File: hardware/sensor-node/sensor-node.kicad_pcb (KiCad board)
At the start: 2 copper layers, 57 x 57 mm, 52 parts, among them J1 CONUFL001-SMD-T, J2 Conn_ARM_JTAG_SWD_10, Q1 PMV250EPEA, U1 TLV61225, U2 TPS27081A, U3 SHT31-DIS, U4 24LC32, U5 MLX90614, U6 ADG633YRU, U7 TSV911RILT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

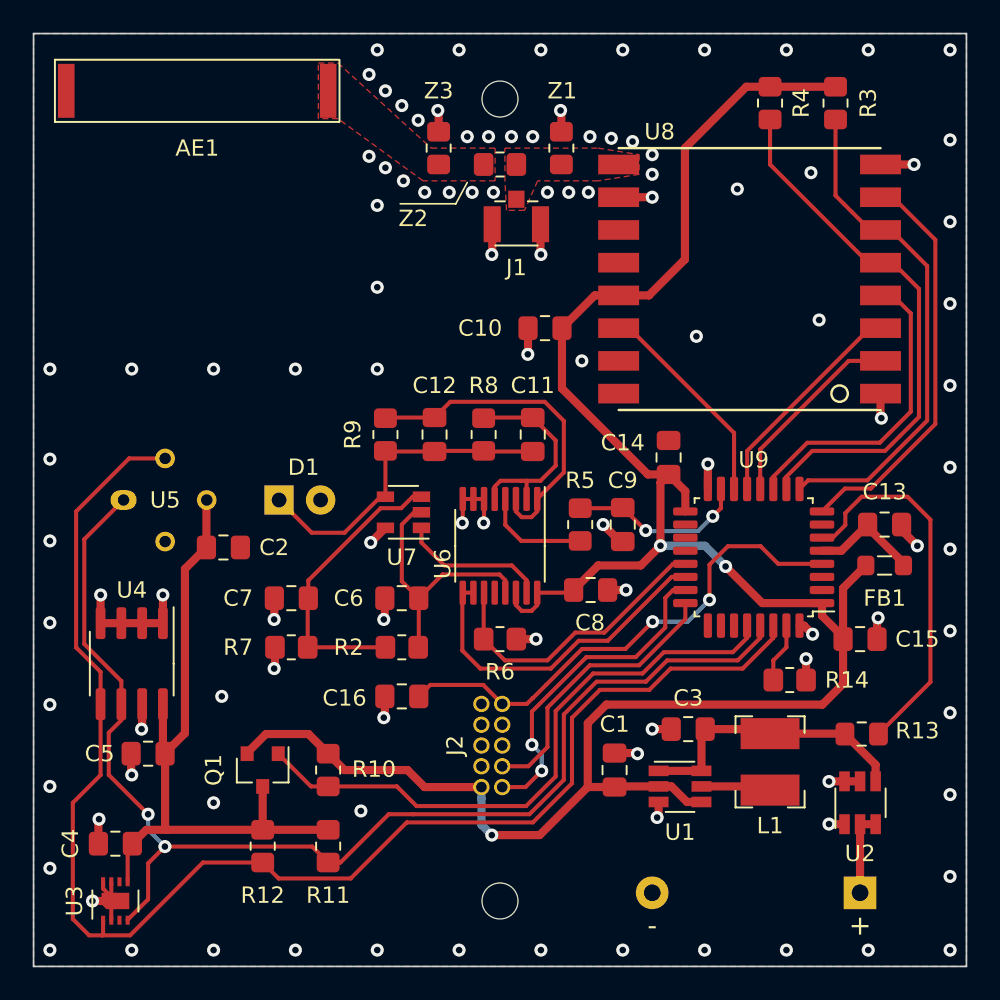
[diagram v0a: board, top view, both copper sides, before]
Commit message: Fix PCB problems for Rev. 2
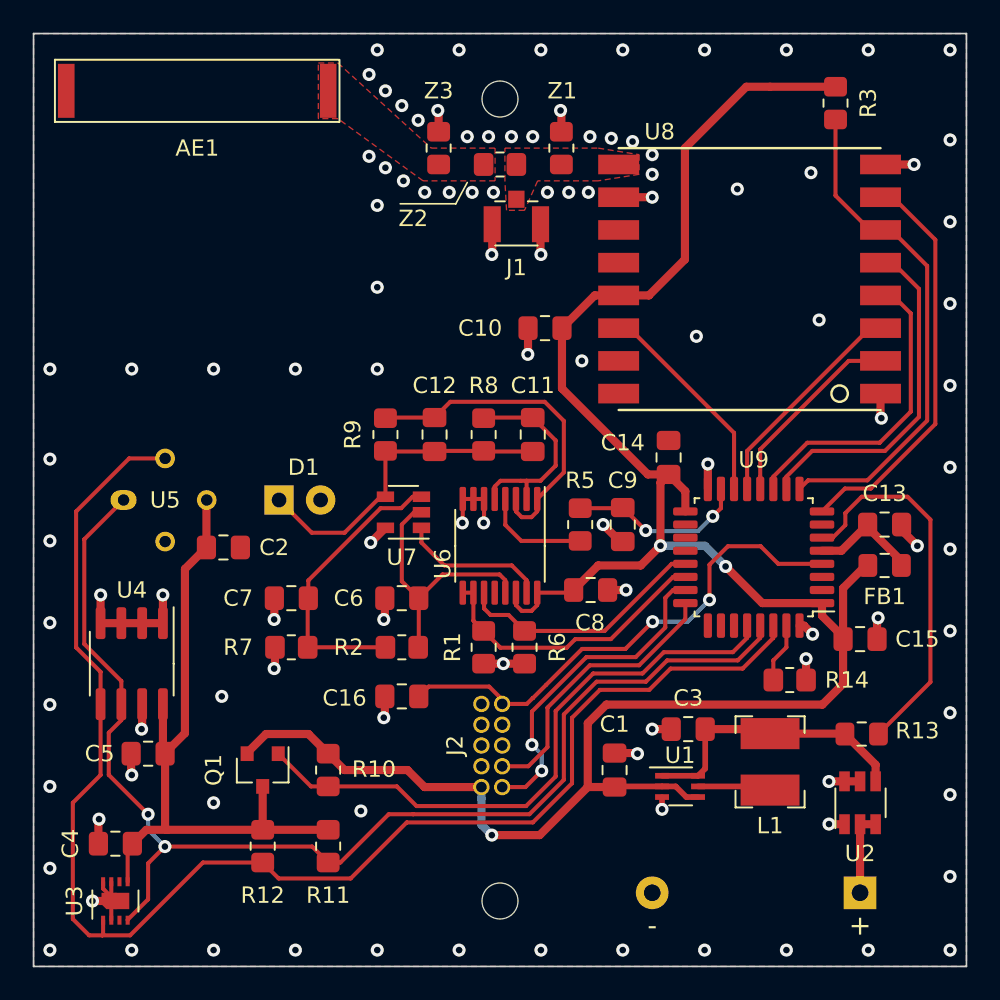
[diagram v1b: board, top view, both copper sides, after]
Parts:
- removed R4: 100k, Resistor_SMD:R_0805_2012Metric_Pad1.20x1.40mm_HandSolder
- added R1: 100k, Resistor_SMD:R_0805_2012Metric_Pad1.20x1.40mm_HandSolder, F.Cu at (127.5, 80.5)
- AE1: value Antenna -> ANT-868-CHP-T
- BT1: value Battery -> Keystone-2468
- D1: value D_Photo -> BPV10
- FB1: value WE 742792040 -> WE742792040; footprint Inductor_SMD:L_0805_2012Metric_Pad1.05x1.20mm_HandSolder -> Inductor_SMD:L_0805_2012Metric_Pad1.15x1.40mm_HandSolder
- J2: value Conn_ARM_JTAG_SWD_10 -> SHF-105-01-L-D-TH
- R6: value 10k -> 100k
- U1: footprint Package_TO_SOT_SMD:TSOT-23-6 -> my-footprints-library:SC-70-6
- moved R6 1.58 mm to (130.0, 80.5), turned to 90 degrees
- moved G*** 0.07 mm to (110.0, 46.5)
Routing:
- net RFM95_NSS: track 33.2 -> 21.9 mm
- net PHOTO_ENABLE: track 18.2 -> 15.5 mm
- net PHOTO_SWITCH: track 20.1 -> 17.8 mm
- net GND: track 58.6 -> 59.7 mm
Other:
- board text added: "Sensor Node Rev. 2"
- board text removed: "Sensor Node Rev. 1"
